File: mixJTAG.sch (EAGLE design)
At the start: 57 parts, among them J1 PLUG-A, J2 CON_HEADER_1X03-PTH, J3 CON_HEADER_2X08, U1 SRV05-4, U2 93LC56B, U3 FT2232HLLQFP, U4 TC2117-800MA, U5 XC2C32A-6VQ44C, U6 SRV05-4, U7 SRV05-4, U8 SRV05-4, U9 SRV05-4, X1 12MHz

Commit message: back up committing
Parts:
- L1, L2, L3: device others:DO3316P -> rcl:L-EUL2012C
- L4: value 600R0.5A -> 600R0.4A; device others:DO3316P -> rcl:L-EUL2012C
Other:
- moved on the sheet: L1, L2, L3, L4
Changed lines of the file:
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@@
 <part name="C16" library="rcl" deviceset="C-EU" device="C0805" value="100n"/>
 <part name="C17" library="rcl" deviceset="C-EU" device="C0805" value="100n"/>
-<part name="L3" library="others" deviceset="DO3316P" device="" value="600R/0.4A"/>
-<part name="L2" library="others" deviceset="DO3316P" device="" value="600R/0.4A"/>
-<part name="L1" library="others" deviceset="DO3316P" device="" value="600R/0.4A"/>
+<part name="L3" library="rcl" deviceset="L-EU" device="L2012C" value="600R/0.4A"/>
+<part name="L2" library="rcl" deviceset="L-EU" device="L2012C" value="600R/0.4A"/>
+<part name="L1" library="rcl" deviceset="L-EU" device="L2012C" value="600R/0.4A"/>
 <part name="GND4" library="bb_supply" deviceset="GND" device=""/>
 <part name="U4" library="bb_ldo" deviceset="TC2117-800MA" device="" value="TC2117-800MA"/>
@@
 <part name="+3V311" library="bb_supply" deviceset="+3V3" device=""/>
 <part name="C25" library="rcl" deviceset="CPOL-US" device="A/3216-18R" value="4.7u"/>
-<part name="L4" library="others" deviceset="DO3316P" device="" value="600R0.5A"/>
+<part name="L4" library="rcl" deviceset="L-EU" device="L2012C" value="600R0.4A"/>
 <part name="U1" library="bb_tvs" deviceset="SRV05-4" device=""/>
 <part name="PCB1" library="bb_pcb" deviceset="PCB_DP_RECTANGLE" device="-50X100"/>
@@
 <instance part="C16" gate="G$1" x="91.44" y="146.05"/>
 <instance part="C17" gate="G$1" x="97.79" y="146.05"/>
-<instance part="L3" gate="G$1" x="63.5" y="118.11"/>
-<instance part="L2" gate="G$1" x="-41.91" y="109.22"/>
-<instance part="L1" gate="G$1" x="-43.18" y="7.62"/>
+<instance part="L3" gate="G$1" x="63.5" y="118.11" rot="R90"/>
+<instance part="L2" gate="G$1" x="-41.91" y="109.22" rot="R90"/>
+<instance part="L1" gate="G$1" x="-43.18" y="7.62" rot="R90"/>
 <instance part="GND4" gate="1" x="-26.67" y="-6.35"/>
 <instance part="U4" gate="G$1" x="91.44" y="118.11"/>
@@
 <instance part="+3V311" gate="G$1" x="172.72" y="124.46"/>
 <instance part="C25" gate="G$1" x="314.96" y="31.75"/>
-<instance part="L4" gate="G$1" x="298.45" y="36.83"/>
+<instance part="L4" gate="G$1" x="298.45" y="36.83" rot="R90"/>
 <instance part="U1" gate="G$1" x="-31.75" y="66.04" rot="R90"/>
 <instance part="PCB1" gate="G$1" x="220.98" y="125.73"/>

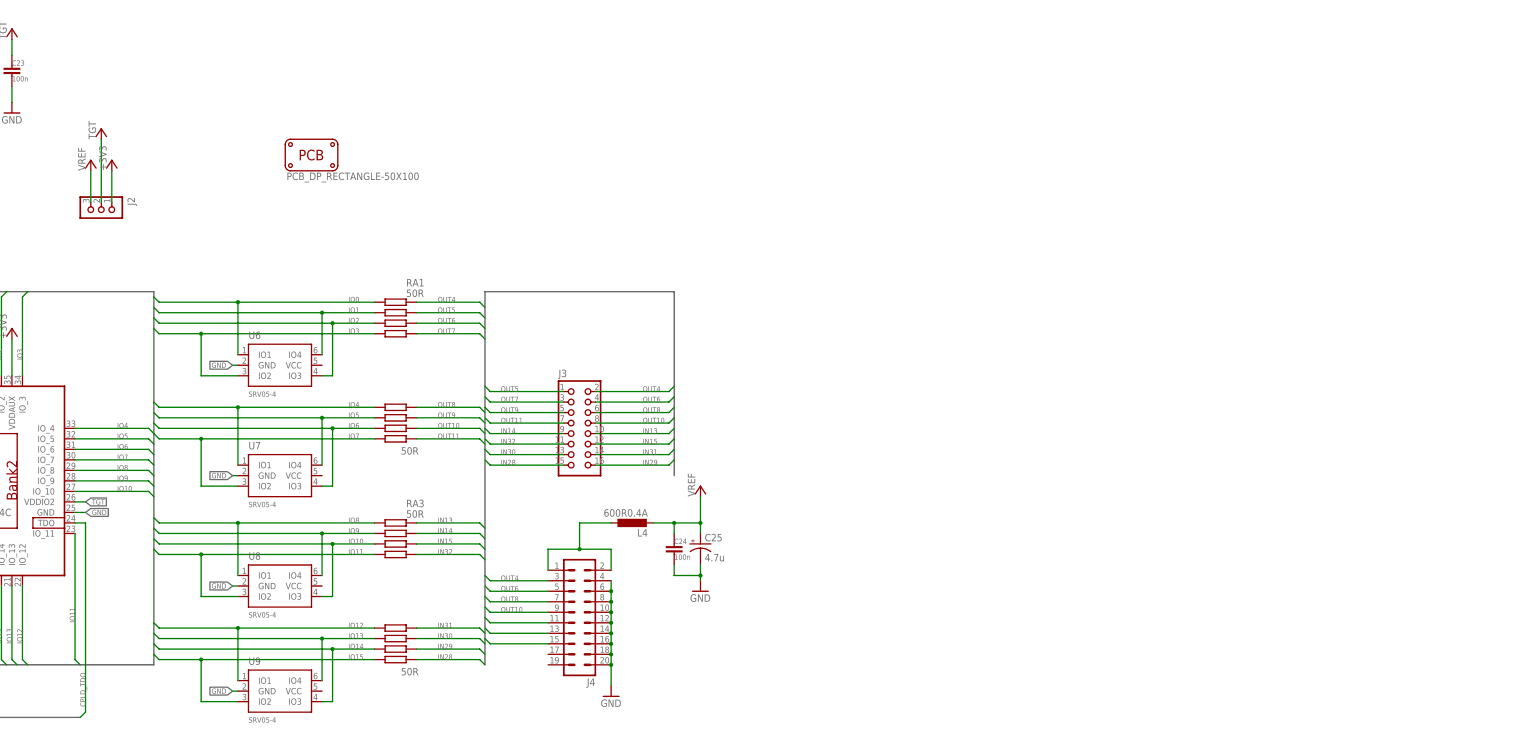
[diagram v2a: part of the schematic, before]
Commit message: add io buffer board
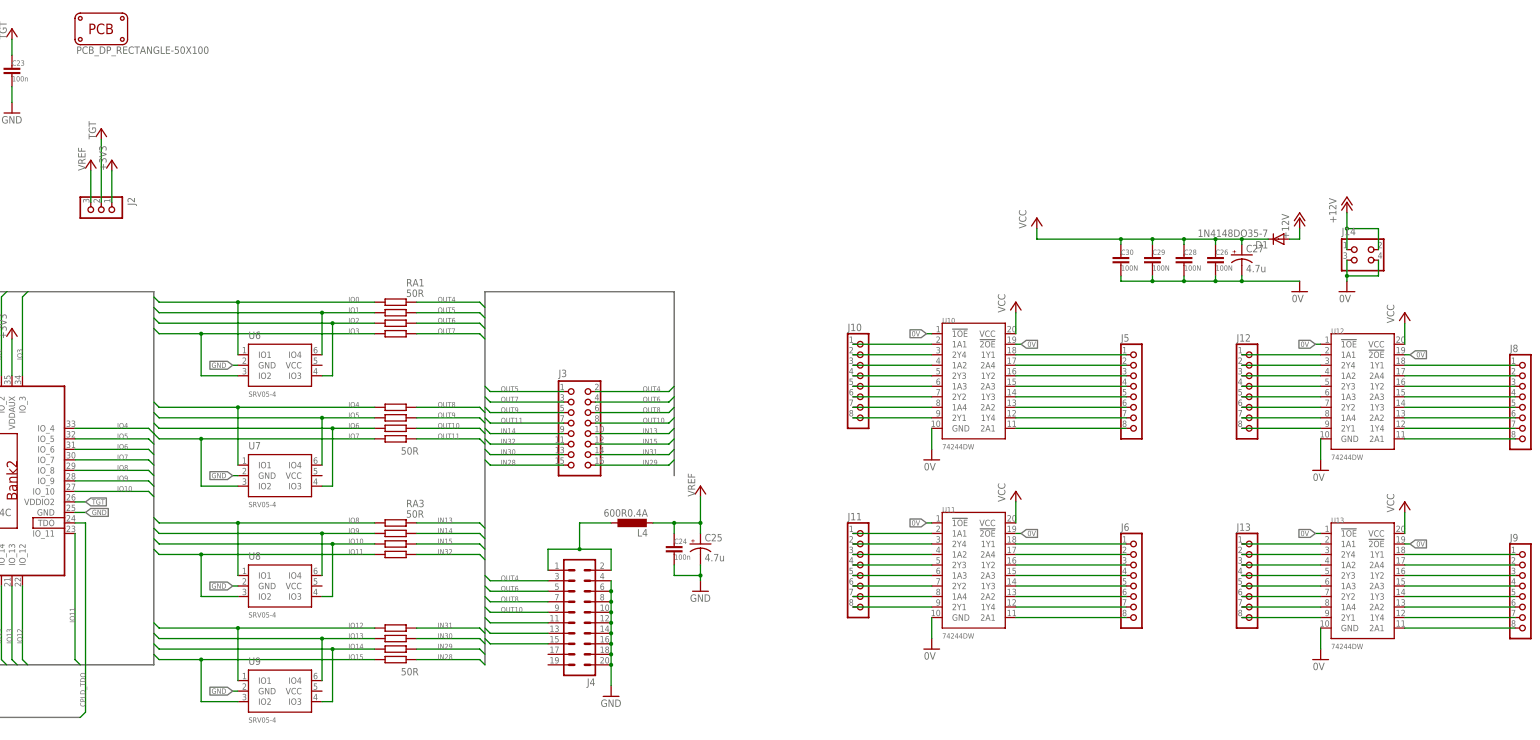
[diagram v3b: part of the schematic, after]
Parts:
- added C26, C28, C29, C30: 100N, rcl:C-EUC0805
- added C27: 4.7u, rcl:CPOL-USSMCA
- added D1: 1N4148DO35-7, diode:1N4148DO35-7
- added J10, J11, J12, J13, J5, J6, J8, J9: CON_HEADER_1X08-PTH, bb_pinheader:CON_HEADER_1X08-PTH
- added J14: CON_HEADER_2X02-PTH, bb_pinheader:CON_HEADER_2X02-PTH
- added U10, U11, U12, U13: 74244DW, bb_74:74244DW
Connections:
- new net +12V: D1.A, J14.1, J14.2
- new net 0V: C26.2, C27.-, C28.2, C29.2, C30.2, J14.3, J14.4, U10.!1OE, U10.!2OE, U10.GND, U11.!1OE, U11.!2OE, U11.GND, U12.!1OE, U12.!2OE, U12.GND, U13.!1OE, U13.!2OE, U13.GND
- new net N$10: J10.5, U10.1A3
- new net N$11: J10.4, U10.2Y3
- new net N$12: J10.3, U10.1A2
- new net N$14: J10.2, U10.2Y4
- new net N$15: J10.1, U10.1A1
- new net N$16: J5.8, U10.2A1
- new net N$17: J5.7, U10.1Y4
- new net N$18: J5.6, U10.2A2
- new net N$19: J5.5, U10.1Y3
- new net N$20: J5.4, U10.2A3
- new net N$21: J5.3, U10.1Y2
- new net N$22: J5.2, U10.2A4
- new net N$23: J5.1, U10.1Y1
- new net N$24: J11.8, U11.2Y1
- new net N$25: J11.7, U11.1A4
- new net N$26: J11.6, U11.2Y2
- new net N$27: J11.5, U11.1A3
- new net N$28: J11.4, U11.2Y3
- new net N$29: J11.3, U11.1A2
- new net N$30: J11.2, U11.2Y4
- new net N$31: J11.1, U11.1A1
- new net N$32: J6.8, U11.2A1
- new net N$33: J6.7, U11.1Y4
- new net N$34: J6.6, U11.2A2
- new net N$35: J6.5, U11.1Y3
- new net N$36: J6.4, U11.2A3
- new net N$37: J6.3, U11.1Y2
- new net N$38: J6.2, U11.2A4
- new net N$39: J6.1, U11.1Y1
- new net N$40: J12.8, U12.2Y1
- new net N$41: J12.7, U12.1A4
- new net N$42: J12.6, U12.2Y2
- new net N$43: J12.5, U12.1A3
- new net N$44: J12.4, U12.2Y3
- new net N$45: J12.3, U12.1A2
- new net N$46: J12.2, U12.2Y4
- new net N$47: J12.1, U12.1A1
- new net N$48: J8.8, U12.2A1
- new net N$49: J8.7, U12.1Y4
- new net N$50: J8.6, U12.2A2
- new net N$51: J8.5, U12.1Y3
- new net N$52: J8.4, U12.2A3
- new net N$53: J8.3, U12.1Y2
- new net N$54: J8.2, U12.2A4
- new net N$55: J8.1, U12.1Y1
- new net N$56: J13.8, U13.2Y1
- new net N$57: J13.7, U13.1A4
- new net N$58: J13.6, U13.2Y2
- new net N$59: J13.5, U13.1A3
- new net N$60: J13.4, U13.2Y3
- new net N$61: J13.3, U13.1A2
- new net N$62: J13.2, U13.2Y4
- new net N$63: J13.1, U13.1A1
- new net N$64: J9.8, U13.2A1
- new net N$65: J9.7, U13.1Y4
- new net N$66: J9.6, U13.2A2
- new net N$67: J9.5, U13.1Y3
- new net N$68: J9.4, U13.2A3
- new net N$69: J9.3, U13.1Y2
- new net N$7: J10.8, U10.2Y1
- new net N$70: J9.2, U13.2A4
- new net N$71: J9.1, U13.1Y1
- new net N$8: J10.7, U10.1A4
- new net N$9: J10.6, U10.2Y2
- new net VCC: C26.1, C27.+, C28.1, C29.1, C30.1, D1.C, U10.VCC, U11.VCC, U12.VCC, U13.VCC

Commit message: change to 0805 current limit resistor
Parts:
- removed J14: CON_HEADER_2X02-PTH, bb_pinheader:CON_HEADER_2X02-PTH
- removed RA1, RA2, RA3, RA4: 50R, bb_ra:4R-N
- added J7: CON_HEADER_1X08-PTH, bb_pinheader:CON_HEADER_1X08-PTH
- added R10, R11, R12, R13, R14, R15, R16, R17, R18, R19, R20, R21, R22, R23, R24, R9: 50R, rcl:R-US_R0805
- C26, C28, C29: value 100N -> 100n
- C27: value 4.7u -> 100n; device rcl:CPOL-USSMCA -> rcl:C-EUC0805
- C30: value 100N -> 4.7u; device rcl:C-EUC0805 -> rcl:CPOL-USA/3216-18R
- J11: value CON_HEADER_1X08-PTH -> CON_HEADER_2X02-PTH; device bb_pinheader:CON_HEADER_1X08-PTH -> bb_pinheader:CON_HEADER_2X02-PTH
- J4: value (none) -> CON_HEADER_2X10-PTH; device bb_ml:ML20 -> bb_pinheader:CON_HEADER_2X10-PTH
- L4: value 600R0.4A -> 600R/0.4A
- LED1: value (none) -> RED
- R3, R7: value 2k -> 2K
- R4, R5, R6: value 2k -> 10K
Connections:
- removed net 0V: C26.2, C27.-, C28.2, C29.2, C30.2, J14.3, J14.4, U10.!1OE, U10.!2OE, U10.GND, U11.!1OE, U11.!2OE, U11.GND, U12.!1OE, U12.!2OE, U12.GND, U13.!1OE, U13.!2OE, U13.GND
- new net GNDA: C26.2, C27.2, C28.2, C29.2, C30.-, J11.3, J11.4, U10.!1OE, U10.!2OE, U10.GNDA, U11.!1OE, U11.!2OE, U11.GNDA, U12.!1OE, U12.!2OE, U12.GNDA, U13.!1OE, U13.!2OE, U13.GNDA
- net +12V: now also J11.1, J11.2; no longer J14.1, J14.2
- net IN13: now also R17.2; no longer RA3.8
- net IN14: now also R18.2; no longer RA3.7
- net IN15: now also R19.2; no longer RA3.6
- net IN28: now also R24.2; no longer RA4.5
- net IN29: now also R23.2; no longer RA4.6
- net IN30: now also R22.2; no longer RA4.7
- net IN31: now also R21.2; no longer RA4.8
- net IN32: now also R20.2; no longer RA3.5
- net IO0: now also R9.1, U6.IO4; no longer RA1.1, U6.IO1
- net IO1: now also R10.1, U6.IO1; no longer RA1.2, U6.IO4
- net IO10: now also R19.1, U8.IO2; no longer RA3.3, U8.IO3
- net IO11: now also R20.1, U8.IO3; no longer RA3.4, U8.IO2
- net IO12: now also R21.1, U9.IO4; no longer RA4.1, U9.IO1
- net IO13: now also R22.1, U9.IO1; no longer RA4.2, U9.IO4
- net IO14: now also R23.1, U9.IO2; no longer RA4.3, U9.IO3
- net IO15: now also R24.1, U9.IO3; no longer RA4.4, U9.IO2
- net IO2: now also R11.1, U6.IO2; no longer RA1.3, U6.IO3
- net IO3: now also R12.1, U6.IO3; no longer RA1.4, U6.IO2
- net IO4: now also R13.1, U7.IO4; no longer RA2.1, U7.IO1
- net IO5: now also R14.1, U7.IO1; no longer RA2.2, U7.IO4
- net IO6: now also R15.1, U7.IO2; no longer RA2.3, U7.IO3
- net IO7: now also R16.1, U7.IO3; no longer RA2.4, U7.IO2
- net IO8: now also R17.1, U8.IO4; no longer RA3.1, U8.IO1
- net IO9: now also R18.1, U8.IO1; no longer RA3.2, U8.IO4
- net N$10: now also J5.5; no longer J10.5
- net N$11: now also J5.4; no longer J10.4
- net N$12: now also J5.3; no longer J10.3
- net N$14: now also J5.2; no longer J10.2
- net N$15: now also J5.1; no longer J10.1
- net N$16: now also J7.8; no longer J5.8
- net N$17: now also J7.7; no longer J5.7
- net N$18: now also J7.6; no longer J5.6
- net N$19: now also J7.5; no longer J5.5
- net N$20: now also J7.4; no longer J5.4
- net N$21: now also J7.3; no longer J5.3
- net N$22: now also J7.2; no longer J5.2
- net N$23: now also J7.1; no longer J5.1
- net N$24: now also J6.8; no longer J11.8
- net N$25: now also J6.7; no longer J11.7
- net N$26: now also J6.6; no longer J11.6
- net N$27: now also J6.5; no longer J11.5
- net N$28: now also J6.4; no longer J11.4
- net N$29: now also J6.3; no longer J11.3
- net N$30: now also J6.2; no longer J11.2
- net N$31: now also J6.1; no longer J11.1
- net N$32: now also J8.8; no longer J6.8
- net N$33: now also J8.7; no longer J6.7
- net N$34: now also J8.6; no longer J6.6
- net N$35: now also J8.5; no longer J6.5
- net N$36: now also J8.4; no longer J6.4
- net N$37: now also J8.3; no longer J6.3
- net N$38: now also J8.2; no longer J6.2
- net N$39: now also J8.1; no longer J6.1
- net N$40: now also J9.8; no longer J12.8
- net N$41: now also J9.7; no longer J12.7
- net N$42: now also J9.6; no longer J12.6
- net N$43: now also J9.5; no longer J12.5
- net N$44: now also J9.4; no longer J12.4
- net N$45: now also J9.3; no longer J12.3
- net N$46: now also J9.2; no longer J12.2
- net N$47: now also J9.1; no longer J12.1
- net N$48: now also J12.8; no longer J8.8
- net N$49: now also J12.7; no longer J8.7
- net N$50: now also J12.6; no longer J8.6
- net N$51: now also J12.5; no longer J8.5
- net N$52: now also J12.4; no longer J8.4
- net N$53: now also J12.3; no longer J8.3
- net N$54: now also J12.2; no longer J8.2
- net N$55: now also J12.1; no longer J8.1
- net N$56: now also J10.8; no longer J13.8
- net N$57: now also J10.7; no longer J13.7
- net N$58: now also J10.6; no longer J13.6
- net N$59: now also J10.5; no longer J13.5
- net N$60: now also J10.4; no longer J13.4
- net N$61: now also J10.3; no longer J13.3
- net N$62: now also J10.2; no longer J13.2
- net N$63: now also J10.1; no longer J13.1
- net N$64: now also J13.8; no longer J9.8
- net N$65: now also J13.7; no longer J9.7
- net N$66: now also J13.6; no longer J9.6
- net N$67: now also J13.5; no longer J9.5
- net N$68: now also J13.4; no longer J9.4
- net N$69: now also J13.3; no longer J9.3
- net N$7: now also J5.8; no longer J10.8
- net N$70: now also J13.2; no longer J9.2
- net N$71: now also J13.1; no longer J9.1
- net N$8: now also J5.7; no longer J10.7
- net N$9: now also J5.6; no longer J10.6
- net OUT10: now also R15.2; no longer RA2.6
- net OUT11: now also R16.2; no longer RA2.5
- net OUT4: now also R9.2; no longer RA1.8
- net OUT5: now also R10.2; no longer RA1.7
- net OUT6: now also R11.2; no longer RA1.6
- net OUT7: now also R12.2; no longer RA1.5
- net OUT8: now also R13.2; no longer RA2.8
- net OUT9: now also R14.2; no longer RA2.7
- net VCC: now also C27.1, C30.+; no longer C27.+, C30.1
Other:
- moved on the sheet: C26, C29, J10, J12, J13, J5, J6, J8, J9, U10, U11
